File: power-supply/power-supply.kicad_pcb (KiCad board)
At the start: 2 copper layers, 70 x 130 mm, 34 parts, among them J1 Barrel_Jack, J2 Output, J3 Output, SW1 SW_SPDT, U1 LM7812_TO220, U2 L7912, U3 L7805

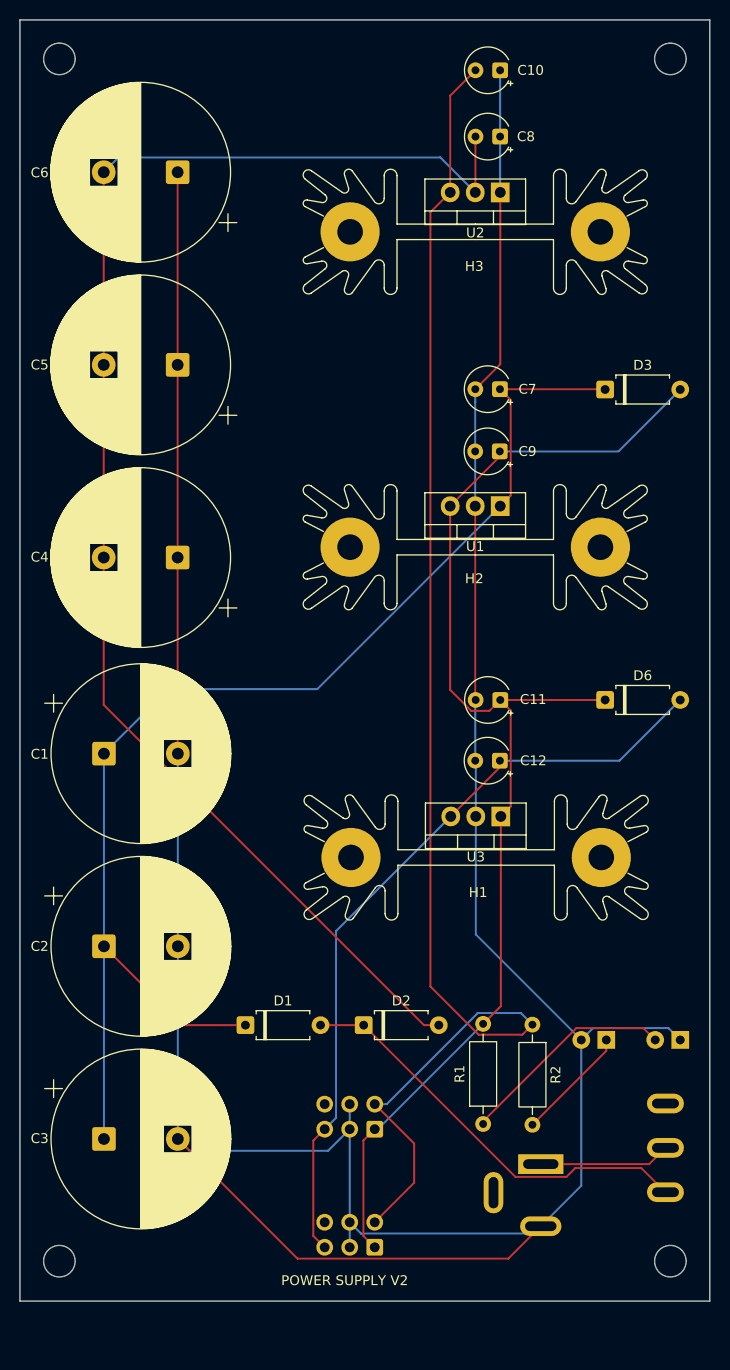
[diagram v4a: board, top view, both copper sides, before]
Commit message: Allow alternative heatsink on power supply
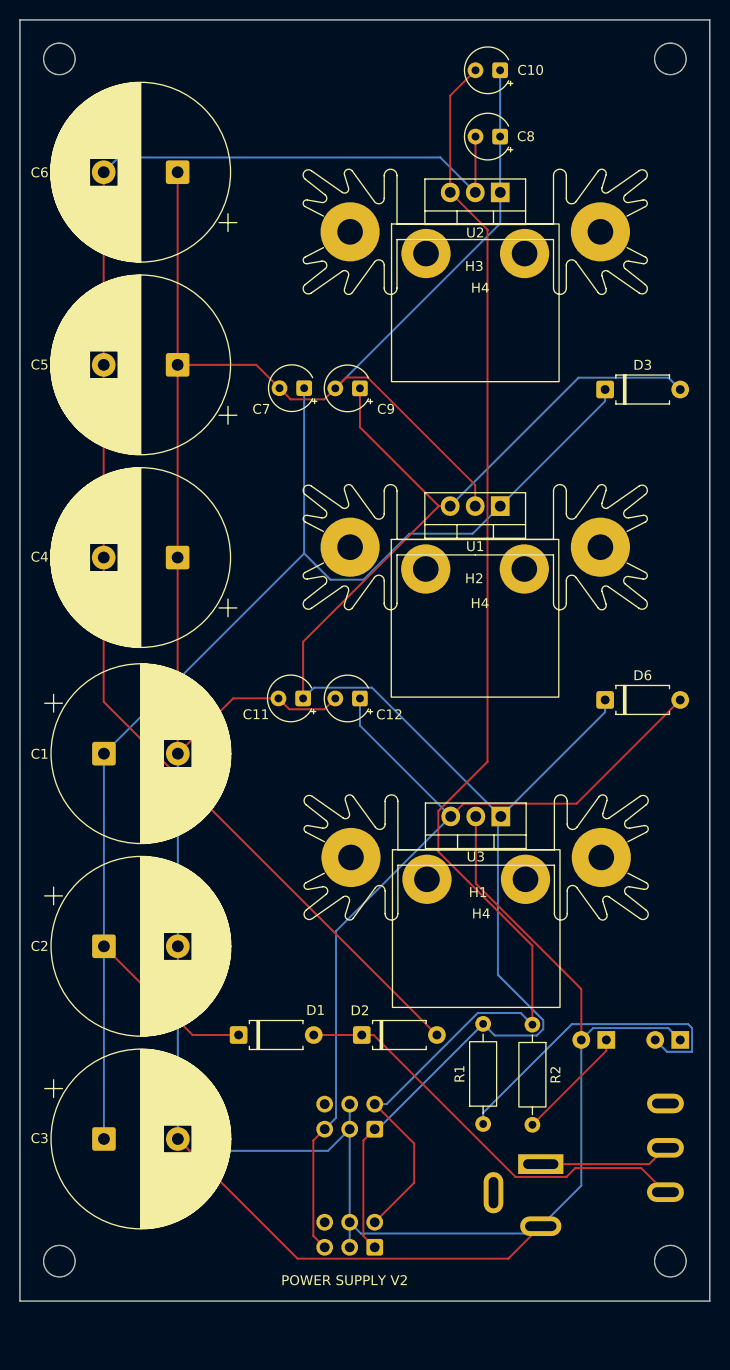
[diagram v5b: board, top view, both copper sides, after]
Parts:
- added H4: heatsink to220, modular2:heatsink to220, F.Cu at (109.2, 61.2)
- added H4: heatsink to220, modular2:heatsink to220, F.Cu at (109.3, 124.7)
- added H4: heatsink to220, modular2:heatsink to220, F.Cu at (109.2, 93.2)
- moved C11 20.0 mm to (91.7, 106.3)
- moved C7 19.9 mm to (91.8, 74.9)
- moved C9 15.6 mm to (97.5, 74.9)
- moved C12 15.5 mm to (97.5, 106.4)
- moved D1 1.21 mm to (85.2, 140.5)
- moved D2 1.02 mm to (97.7, 140.5)
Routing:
- net Net-(D3-A): track 127.1 -> 171.9 mm
- net GND: track 331.4 -> 352.2 mm
- net Net-(D6-A): track 78.5 -> 93.9 mm
- net Net-(D1-K): track 131.7 -> 143.2 mm
- net Net-(D4-A): track 22.1 -> 33.1 mm
- net Net-(J2-Pin_2): track 143.3 -> 141.1 mm

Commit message: Various improvements
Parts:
- added G***: LOGO, modular2:ibis-small, B.Cu at (78.0, 160.5)
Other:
- board text added: "POWER SUPPLY V3"
- board text removed: "POWER SUPPLY V2"

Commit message: Various improvements
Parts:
- added J4: Output, Connector_IDC:IDC-Header_2x03_P2.54mm_Vertical, B.Cu at (94.0, 140.0)
- moved D2 19.3 mm to (86.0, 125.1), turned to 90 degrees
- moved SW1 8.45 mm to (128.5, 152.0)
- moved J2 6.37 mm to (93.9, 165.9), turned to -90 degrees
- moved J3 5.81 mm to (93.9, 152.9), turned to -90 degrees
- moved REF** 5.05 mm to (67.0, 168.5)
- moved REF** 5.05 mm to (129.0, 168.5)
- moved D1 4.88 mm to (86.0, 145.3), turned to 90 degrees
- moved J1 4.55 mm to (115.8, 158.2)
- moved G*** 2.00 mm to (78.0, 162.5)
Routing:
- net Net-(D2-A): track 147.0 -> 118.1 mm
- net Net-(D1-A): track 43.0 -> 62.8 mm
- net Net-(D3-A): track 171.9 -> 188.2 mm
- net Net-(J2-Pin_2): track 141.1 -> 155.6 mm
- net Net-(D6-A): track 93.9 -> 103.6 mm
- net Net-(SW1-B): track 13.3 -> 15.2 mm
- net Net-(D1-K): track 143.2 -> 141.8 mm
- net GND: track 352.2 -> 351.5 mm
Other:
- board size 70 x 130 mm -> 70 x 135 mm
- board text added: "OFF"
- board text added: "ON"

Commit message: Update gerbers
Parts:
- turned G*** to 0 degrees
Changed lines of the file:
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@@
 		(tags "LED")
 		(property "Reference" "D5"
-			(at 1.04 -4.05 0)
+			(at 0.94 4.3 270)
 			(layer "B.SilkS")
 			(effects
@@
 		(tags "LED")
 		(property "Reference" "D4"
-			(at 1.54 -4.05 0)
+			(at 1.4 4.3 90)
 			(layer "B.SilkS")
 			(effects
@@
 		(tags "connector barrel jack")
 		(property "Reference" "J1"
-			(at 0 2.5 0)
+			(at 0 2.5 90)
 			(layer "B.SilkS")
 			(effects
@@
 	(footprint "modular2:ibis-small"
 		(layer "B.Cu")
-		(at 78 162.5 180)
+		(at 78 162.5)
 		(property "Reference" "G***"
 			(at 0 0 0)
@@
 		(at 128.5 152 180)
 		(property "Reference" "SW1"
-			(at 6 0 -0)
+			(at 6 0 0)
 			(unlocked yes)
 			(layer "F.SilkS")
@@
 	)
 	(gr_text "POWER SUPPLY V3"
-		(at 85 171.5 -0)
+		(at 71 168.7 180)
 		(layer "B.SilkS")
 		(effects
